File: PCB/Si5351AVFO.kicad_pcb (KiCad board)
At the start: 4 copper layers, 100 x 65 mm, 127 parts, among them J1 USB_C_Receptacle, J2 SMA CLK0, J3 SMA CLK1, J4 SMA CLK2, J5 UPDI, SW1 EC11E18244A5, SW2 BAND, SW3 STEP, SW4 MENU, U1 LP2985-3.3, U2 Si5351A-B-GT, U3 CP2102N-A02-GQFN24, U4 ATtiny3226-SU, U5 LP2985-3.3, X1 25MHz TCXO

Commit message: WIP: partial PCB review fixes (interrupted pass)
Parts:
- added C26: 100n, Capacitor_SMD:C_0402_1005Metric, F.Cu at (172.5, 131.4)
- added C27: 10u, Capacitor_SMD:C_0805_2012Metric, F.Cu at (182.3, 134.6)
- added C28: 100n, Capacitor_SMD:C_0805_2012Metric, F.Cu at (182.3, 136.6)
- added FID1: Fiducial, Fiducial:Fiducial_1mm_Mask2mm, F.Cu at (103.0, 109.0)
- added FID2: Fiducial, Fiducial:Fiducial_1mm_Mask2mm, F.Cu at (196.0, 140.0)
- added FID3: Fiducial, Fiducial:Fiducial_1mm_Mask2mm, F.Cu at (104.0, 152.0)
- R100, R120, R140: footprint Resistor_SMD:R_0805_2012Metric -> Resistor_SMD:R_0402_1005Metric
- SW2: value BAND -> SOFT1
- SW3: value STEP -> SOFT2
- SW4: value MENU -> SOFT3
- moved R100 11.0 mm to (169.0, 132.2), turned to 180 degrees
- moved R140 9.12 mm to (174.9, 131.9)
- moved C4 2.51 mm to (169.6, 136.2), turned to 90 degrees
- moved R120 2.49 mm to (171.0, 131.5)
- moved D1 1.90 mm to (116.0, 110.3)
- moved U2 1.56 mm to (172.0, 135.3), turned to 90 degrees
- turned C6 to -90 degrees
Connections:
- net /MCU and UI/BTN_BAND renamed /MCU and UI/BTN_S1
- net /MCU and UI/BTN_BAND_SW renamed /MCU and UI/BTN_S1_SW
- net /MCU and UI/BTN_MENU renamed /MCU and UI/BTN_S3
- net /MCU and UI/BTN_MENU_SW renamed /MCU and UI/BTN_S3_SW
- net /MCU and UI/BTN_STEP renamed /MCU and UI/BTN_S2
- net /MCU and UI/BTN_STEP_SW renamed /MCU and UI/BTN_S2_SW
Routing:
- net +3V3_CLK: track 55.2 -> 30.2 mm, vias 2 -> 5
- net I2C_SDA: track 55.4 -> 33.7 mm, vias 3 -> 2
- net /Synth and RF outputs/CLK0: track 22.8 -> 2.44 mm, vias 2 -> 0
- net +3V3D: track 138.3 -> 119.5 mm
- net /Synth and RF outputs/CLK2: track 15.9 -> 2.16 mm, vias 2 -> 0
- net +5V: track 79.9 -> 68.9 mm, vias 2 -> 0
- net /Power and USB/CP_RST: track 12.1 -> 1.94 mm, vias 3 -> 0
- net /Power and USB/CP_VBUS_SENSE: track 11.5 -> 1.40 mm, vias 2 -> 0
- net Net-(C100-Pad1): track 2.96 -> 12.3 mm
- net I2C_SCL: track 35.7 -> 44.8 mm
- net /Power and USB/USB_DP: track 17.6 -> 25.9 mm
- net /MCU and UI/ENC_B: track 9.59 -> 17.5 mm, vias 0 -> 2
- net Net-(C140-Pad1): track 2.96 -> 10.0 mm
- net /MCU and UI/BTN_S3_SW: track 29.5 -> 22.7 mm
- net MCU_TX: track 59.8 -> 65.9 mm
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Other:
- board text added: "Controlled impedance 50 ohm, L1/L2, 0.31/0.20 (CPWG, RF50) per JLC calculator"
- board text added: "FAB NOTES: JLC04161H-7628 4L 1.6mm, 1oz outer"
- board text added: "U3 thermal-pad vias: tented both sides + filled (epoxy)"

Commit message: PCB: C27 10u/C28 100n at FB1 output (+3V3_CLK), reroute +3V3_CLK FB1->U2 on In2/B.Cu; C26 at VDDO pin 7, C4 at VDD pin 1
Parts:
- moved C27 48.5 mm to (143.9, 104.9)
- moved C28 48.4 mm to (143.9, 107.0)
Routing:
- net +3V3_CLK: track 30.2 -> 66.0 mm
- net GND: track 65.2 -> 67.2 mm, vias 320 -> 318
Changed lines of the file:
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@@
 	(footprint "Capacitor_SMD:C_0805_2012Metric"
 		(layer "F.Cu")
-		(at 182.3 134.6)
+		(at 143.95 104.9)
 		(descr "Capacitor SMD 0805 (2012 Metric), square (rectangular) end terminal, IPC-7351 nominal, (Body size source: IPC-SM-782 page 76, https://www.pcb-3d.com/wordpress/wp-content/uploads/ipc-sm-782a_amendment_1_and_2.pdf, https://docs.google.com/spreadsheets/d/1BsfQQcO9C6DZCsRaXUlFlo91Tg2WpOkGARC1WS5S8t0/edit?usp=sharing)")
 		(tags "capacitor")
@@
 	(footprint "Capacitor_SMD:C_0805_2012Metric"
 		(layer "F.Cu")
-		(at 182.3 136.6)
+		(at 143.95 107)
 		(descr "Capacitor SMD 0805 (2012 Metric), square (rectangular) end terminal, IPC-7351 nominal, (Body size source: IPC-SM-782 page 76, https://www.pcb-3d.com/wordpress/wp-content/uploads/ipc-sm-782a_amendment_1_and_2.pdf, https://docs.google.com/spreadsheets/d/1BsfQQcO9C6DZCsRaXUlFlo91Tg2WpOkGARC1WS5S8t0/edit?usp=sharing)")
 		(tags "capacitor")
@@
 	)
 	(segment
+		(start 144.9 107)
+		(end 145.9 107)
+		(width 0.4)
+		(layer "F.Cu")
+		(net "GND")
+	)
+	(segment
 		(start 138.45 114)
 		(end 139.399999 114)
@@
 	)
 	(segment
+		(start 144.9 104.9)
+		(end 145.9 104.9)
+		(width 0.4)
+		(layer "F.Cu")
+		(net "GND")
+	)
+	(segment
 		(start 136.2 163.25)
 		(end 134.75 163.25)
@@
 	)
 	(via
-		(at 184.799999 133.8)
-		(size 0.6)
-		(drill 0.3)
-		(layers "F.Cu" "B.Cu")
-		(locked yes)
-		(net "GND")
-	)
-	(via
 		(at 176.799999 137)
 		(size 0.6)
@@
 	)
 	(via
-		(at 184.2 134.6)
-		(size 0.6)
-		(drill 0.3)
-		(layers "F.Cu" "B.Cu")
-		(locked yes)
-		(net "GND")
-	)
-	(via
 		(at 179.125 111.25)
 		(size 0.6)
@@
 	)
 	(via
+		(at 145.9 104.9)
+		(size 0.6)
+		(drill 0.3)
+		(layers "F.Cu" "B.Cu")
+		(net "GND")
+	)
+	(via
 		(at 179.999999 117.8)
 		(size 0.6)
@@
 	)
 	(via
+		(at 145.9 107)
+		(size 0.6)
+		(drill 0.3)
+		(layers "F.Cu" "B.Cu")
+		(net "GND")
+	)
+	(via
 		(at 165.6 117.8)
 		(size 0.6)
@@
 	)
 	(via
-		(at 184.799999 135.4)
-		(size 0.6)
-		(drill 0.3)
-		(layers "F.Cu" "B.Cu")
-		(locked yes)
-		(net "GND")
-	)
-	(via
 		(at 167.2 125.8)
 		(size 0.6)
@@
 	)
 	(via
-		(at 184.2 136.6)
-		(size 0.6)
-		(drill 0.3)
-		(layers "F.Cu" "B.Cu")
-		(locked yes)
-		(net "GND")
-	)
-	(via
 		(at 156 109.8)
 		(size 0.6)
@@
 	)
 	(segment
-		(start 180.1 135.6)
-		(end 181.35 135.6)
-		(width 0.4)
-		(locked yes)
-		(layer "F.Cu")
-		(net "+3V3_CLK")
-	)
-	(segment
-		(start 143 110.2125)
-		(end 143 109.325)
+		(start 143 110.21)
+		(end 143 104.9)
 		(width 0.4)
-		(locked yes)
 		(layer "F.Cu")
 		(net "+3V3_CLK")
@@
 	)
 	(segment
-		(start 181.35 134.6)
-		(end 181.35 136.6)
+		(start 143 104.9)
+		(end 143 103.6)
 		(width 0.4)
-		(locked yes)
 		(layer "F.Cu")
 		(net "+3V3_CLK")
@@
 	)
 	(via
-		(at 168.4 137.4)
+		(at 154.6 126.6)
 		(size 0.6)
 		(drill 0.3)
 		(layers "F.Cu" "B.Cu")
-		(locked yes)
 		(net "+3V3_CLK")
 	)
 	(via
-		(at 180.1 135.6)
+		(at 143 103.6)
 		(size 0.6)
 		(drill 0.3)
 		(layers "F.Cu" "B.Cu")
-		(locked yes)
 		(net "+3V3_CLK")
 	)
 	(via
-		(at 163.65 135.15)
+		(at 168.4 137.4)
 		(size 0.6)
 		(drill 0.3)
@@
 	)
 	(via
-		(at 143 109.325)
+		(at 163.65 135.15)
 		(size 0.6)
 		(drill 0.3)
@@
 	)
 	(segment
+		(start 160 132.6)
+		(end 161.2 132.6)
+		(width 0.3)
+		(layer "B.Cu")
+		(net "+3V3_CLK")
+	)
+	(segment
+		(start 159 131.4)
+		(end 159 131.6)
+		(width 0.3)
+		(layer "B.Cu")
+		(net "+3V3_CLK")
+	)
+	(segment
+		(start 154.6 126.6)
+		(end 159 131.4)
+		(width 0.3)
+		(layer "B.Cu")
+		(net "+3V3_CLK")
+	)
+	(segment
+		(start 159 131.6)
+		(end 160 132.6)
+		(width 0.3)
+		(layer "B.Cu")
+		(net "+3V3_CLK")
+	)
+	(segment
+		(start 163.4 135)
+		(end 163.6 135.2)
+		(width 0.3)
+		(layer "B.Cu")
+		(net "+3V3_CLK")
+	)
+	(segment
+		(start 161.2 132.6)
+		(end 163.4 134.8)
+		(width 0.3)
+		(layer "B.Cu")
+		(net "+3V3_CLK")
+	)
+	(segment
+		(start 163.4 134.8)
+		(end 163.4 135)
+		(width 0.3)
+		(layer "B.Cu")
+		(net "+3V3_CLK")
+	)
+	(segment
+		(start 147.2 108)
+		(end 150.8 111.6)
+		(width 0.3)
+		(layer "In2.Cu")
+		(net "+3V3_CLK")
+	)
+	(segment
+		(start 153.6 125.4)
+		(end 153.6 126.6)
+		(width 0.3)
+		(layer "In2.Cu")
+		(net "+3V3_CLK")
+	)
+	(segment
+		(start 152.4 124.2)
+		(end 153.6 125.4)
+		(width 0.3)
+		(layer "In2.Cu")
+		(net "+3V3_CLK")
+	)
+	(segment
+		(start 146 106.2)
+		(end 146.2 106.4)
+		(width 0.3)
+		(layer "In2.Cu")
+		(net "+3V3_CLK")
+	)
+	(segment
 		(start 163.65 135.15)
 		(end 166.15 135.15)
@@
 	)
 	(segment
-		(start 172.7446 134.3554)
-		(end 172.5 134.6)
+		(start 153.6 126.6)
+		(end 154.6 126.6)
 		(width 0.3)
 		(layer "In2.Cu")
@@
 	)
 	(segment
-		(start 175.7767 134.5101)
-		(end 174.4899 134.5101)
+		(start 145.6 106.2)
+		(end 146 106.2)
 		(width 0.3)
 		(layer "In2.Cu")
@@
 	)
 	(segment
-		(start 174.4899 134.5101)
-		(end 174.2177 134.2379)
+		(start 166.15 135.15)
+		(end 168.4 137.4)
 		(width 0.3)
 		(layer "In2.Cu")
@@
 	)
 	(segment
-		(start 166.15 135.15)
-		(end 168.4 137.4)
+		(start 146.2 106.4)
+		(end 146.4 106.4)
 		(width 0.3)
 		(layer "In2.Cu")
@@
 	)
 	(segment
-		(start 178.9202 134.4202)
-		(end 175.8666 134.4202)
+		(start 168.4 137.4)
+		(end 171.2 134.6)
 		(width 0.3)
 		(layer "In2.Cu")
@@
 	)
 	(segment
-		(start 174.2177 134.2379)
-		(end 173.8851 134.2379)
-		(width 0.225)
+		(start 152.4 124)
+		(end 152.4 124.2)
+		(width 0.3)
 		(layer "In2.Cu")
 		(net "+3V3_CLK")
 	)
 	(segment
-		(start 173.8851 134.2379)
-		(end 173.7676 134.3554)
-		(width 0.225)
+		(start 143 103.6)
+		(end 145.6 106.2)
+		(width 0.3)
 		(layer "In2.Cu")
 		(net "+3V3_CLK")
 	)
 	(segment
-		(start 180.1 135.6)
-		(end 178.9202 134.4202)
+		(start 147.2 107.2)
+		(end 147.2 108)
 		(width 0.3)
 		(layer "In2.Cu")
@@
 	)
 	(segment
-		(start 168.4 137.4)
-		(end 171.2 134.6)
+		(start 150.8 122.4)
+		(end 152.4 124)
 		(width 0.3)
 		(layer "In2.Cu")
@@
 	)
 	(segment
-		(start 173.7676 134.3554)
-		(end 172.7446 134.3554)
+		(start 146.4 106.4)
+		(end 147.2 107.2)
 		(width 0.3)
 		(layer "In2.Cu")
@@
 	)
 	(segment
-		(start 175.8666 134.4202)
-		(end 175.7767 134.5101)
+		(start 150.8 111.6)
+		(end 150.8 122.4)
 		(width 0.3)
 		(layer "In2.Cu")

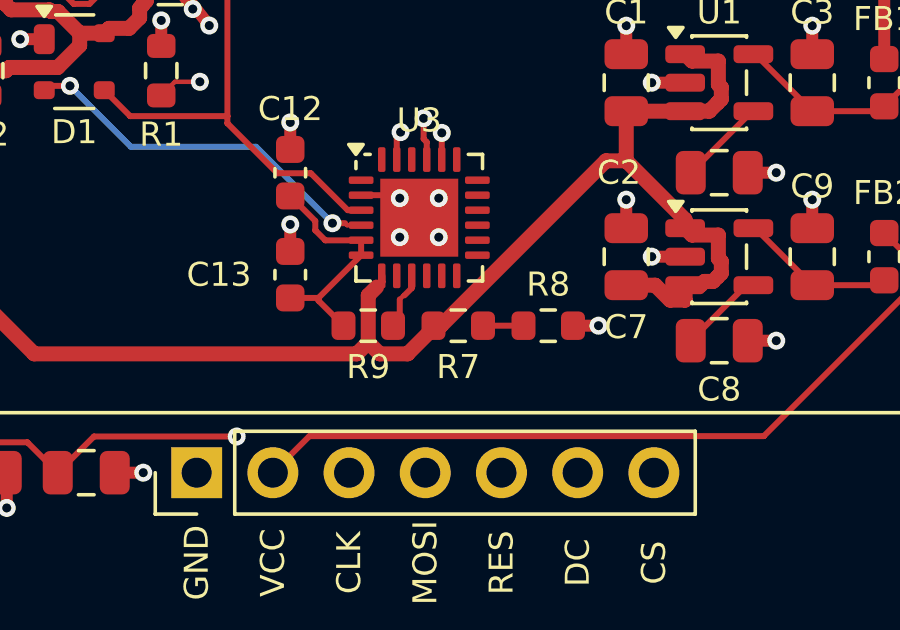
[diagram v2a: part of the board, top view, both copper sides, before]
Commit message: PCB: connect CP_VBUS_SENSE (U3.8) via B.Cu hop, tighten CP_RST escape; DRC 0 unconnected, 0 clearance
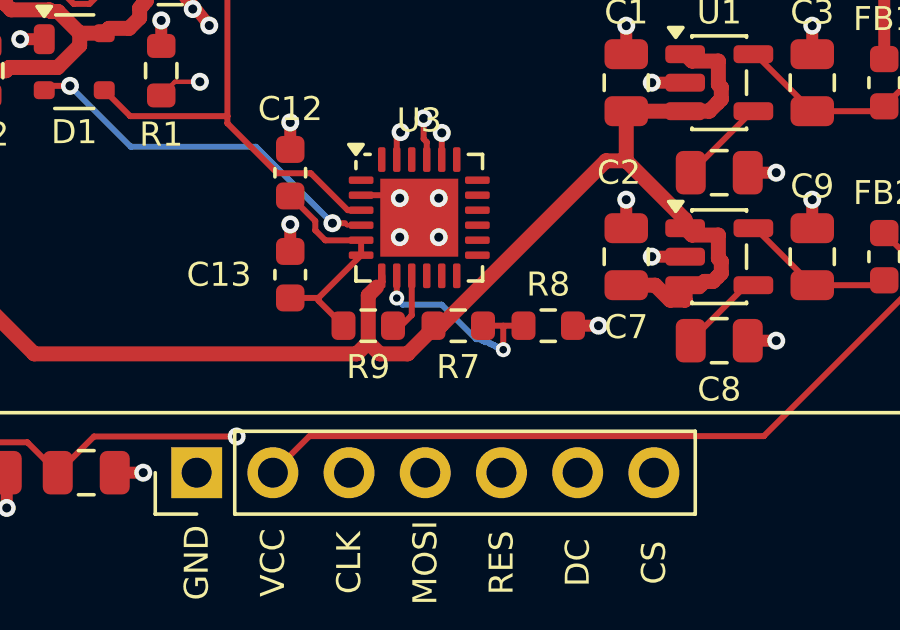
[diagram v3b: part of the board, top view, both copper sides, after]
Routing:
- net /Power and USB/CP_VBUS_SENSE: track 1.40 -> 7.23 mm, vias 0 -> 2
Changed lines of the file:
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@@
+	)
+	(segment
+		(start 126.75 117.44)
+		(end 126.75 118.18)
+		(width 0.2)
+		(layer "F.Cu")
+		(net "/Power and USB/CP_VBUS_SENSE")
 	)
 	(segment
@@
 		(width 0.2)
 		(layer "F.Cu")
+		(net "/Power and USB/CP_VBUS_SENSE")
+	)
+	(segment
+		(start 130.3 119.1)
+		(end 130.3 119.9)
+		(width 0.2)
+		(layer "F.Cu")
+		(net "/Power and USB/CP_VBUS_SENSE")
+	)
+	(via
+		(at 130.3 119.9)
+		(size 0.5)
+		(drill 0.25)
+		(layers "F.Cu" "B.Cu")
+		(net "/Power and USB/CP_VBUS_SENSE")
+	)
+	(via
+		(at 126.75 118.18)
+		(size 0.5)
+		(drill 0.25)
+		(layers "F.Cu" "B.Cu")
+		(net "/Power and USB/CP_VBUS_SENSE")
+	)
+	(segment
+		(start 130 119.75)
+		(end 130.05 119.8)
+		(width 0.2)
+		(layer "B.Cu")
+		(net "/Power and USB/CP_VBUS_SENSE")
+	)
+	(segment
+		(start 129.9 119.7)
+		(end 129.949999 119.75)
+		(width 0.2)
+		(layer "B.Cu")
+		(net "/Power and USB/CP_VBUS_SENSE")
+	)
+	(segment
+		(start 126.95 118.4)
+		(end 128.25 118.4)
+		(width 0.2)
+		(layer "B.Cu")
+		(net "/Power and USB/CP_VBUS_SENSE")
+	)
+	(segment
+		(start 126.8 118.3)
+		(end 126.85 118.3)
+		(width 0.2)
+		(layer "B.Cu")
+		(net "/Power and USB/CP_VBUS_SENSE")
+	)
+	(segment
+		(start 129.699999 119.65)
+		(end 129.8 119.65)
+		(width 0.2)
+		(layer "B.Cu")
+		(net "/Power and USB/CP_VBUS_SENSE")
+	)
+	(segment
+		(start 130.1 119.8)
+		(end 130.15 119.85)
+		(width 0.2)
+		(layer "B.Cu")
+		(net "/Power and USB/CP_VBUS_SENSE")
+	)
+	(segment
+		(start 130.25 119.85)
+		(end 130.3 119.9)
+		(width 0.2)
+		(layer "B.Cu")
+		(net "/Power and USB/CP_VBUS_SENSE")
+	)
+	(segment
+		(start 129.6 119.6)
+		(end 129.65 119.6)
+		(width 0.2)
+		(layer "B.Cu")
+		(net "/Power and USB/CP_VBUS_SENSE")
+	)
+	(segment
+		(start 130.15 119.85)
+		(end 130.25 119.85)
+		(width 0.2)
+		(layer "B.Cu")
+		(net "/Power and USB/CP_VBUS_SENSE")
+	)
+	(segment
+		(start 126.85 118.3)
+		(end 126.95 118.4)
+		(width 0.2)
+		(layer "B.Cu")
+		(net "/Power and USB/CP_VBUS_SENSE")
+	)
+	(segment
+		(start 128.25 118.4)
+		(end 129.4 119.55)
+		(width 0.2)
+		(layer "B.Cu")
+		(net "/Power and USB/CP_VBUS_SENSE")
+	)
+	(segment
+		(start 126.75 118.18)
+		(end 126.8 118.3)
+		(width 0.2)
+		(layer "B.Cu")
+		(net "/Power and USB/CP_VBUS_SENSE")
+	)
+	(segment
+		(start 129.55 119.55)
+		(end 129.6 119.6)
+		(width 0.2)
+		(layer "B.Cu")
+		(net "/Power and USB/CP_VBUS_SENSE")
+	)
+	(segment
+		(start 129.8 119.65)
+		(end 129.85 119.7)
+		(width 0.2)
+		(layer "B.Cu")
+		(net "/Power and USB/CP_VBUS_SENSE")
+	)
+	(segment
+		(start 129.85 119.7)
+		(end 129.9 119.7)
+		(width 0.2)
+		(layer "B.Cu")
+		(net "/Power and USB/CP_VBUS_SENSE")
+	)
+	(segment
+		(start 129.65 119.6)
+		(end 129.699999 119.65)
+		(width 0.2)
+		(layer "B.Cu")
+		(net "/Power and USB/CP_VBUS_SENSE")
+	)
+	(segment
+		(start 129.949999 119.75)
+		(end 130 119.75)
+		(width 0.2)
+		(layer "B.Cu")
+		(net "/Power and USB/CP_VBUS_SENSE")
+	)
+	(segment
+		(start 130.05 119.8)
+		(end 130.1 119.8)
+		(width 0.2)
+		(layer "B.Cu")
+		(net "/Power and USB/CP_VBUS_SENSE")
+	)
+	(segment
+		(start 129.4 119.55)
+		(end 129.55 119.55)
+		(width 0.2)
+		(layer "B.Cu")
 		(net "/Power and USB/CP_VBUS_SENSE")
 	)
@@
 	)
 	(segment
-		(start 126.625 119.1)
-		(end 126.8496 118.8754)
+		(start 127.25 117.44)
+		(end 127.25 118.75)
 		(width 0.2)
 		(layer "F.Cu")
@@
 	)
 	(segment
-		(start 126.9804 118.0905)
-		(end 127.0056 118.0905)
-		(width 0.15)
+		(start 127.25 118.75)
+		(end 126.9 119.1)
+		(width 0.2)
 		(layer "F.Cu")
 		(net "/Power and USB/CP_RST")
 	)
 	(segment
-		(start 126.8496 118.2213)
-		(end 126.9804 118.0905)
-		(width 0.15)
-		(layer "F.Cu")
-		(net "/Power and USB/CP_RST")
-	)
-	(segment
-		(start 127.0056 118.0905)
-		(end 127.25 117.8461)
-		(width 0.2)
-		(layer "F.Cu")
-		(net "/Power and USB/CP_RST")
-	)
-	(segment
-		(start 127.25 117.8461)
-		(end 127.25 117.4375)
-		(width 0.2)
-		(layer "F.Cu")
-		(net "/Power and USB/CP_RST")
-	)
-	(segment
-		(start 126.8496 118.8754)
-		(end 126.8496 118.2213)
-		(width 0.2)
-		(layer "F.Cu")
+		(start 126.9 119.1)
+		(end 126.625 119.1)
+		(width 0.2)
+		(layer "F.Cu")

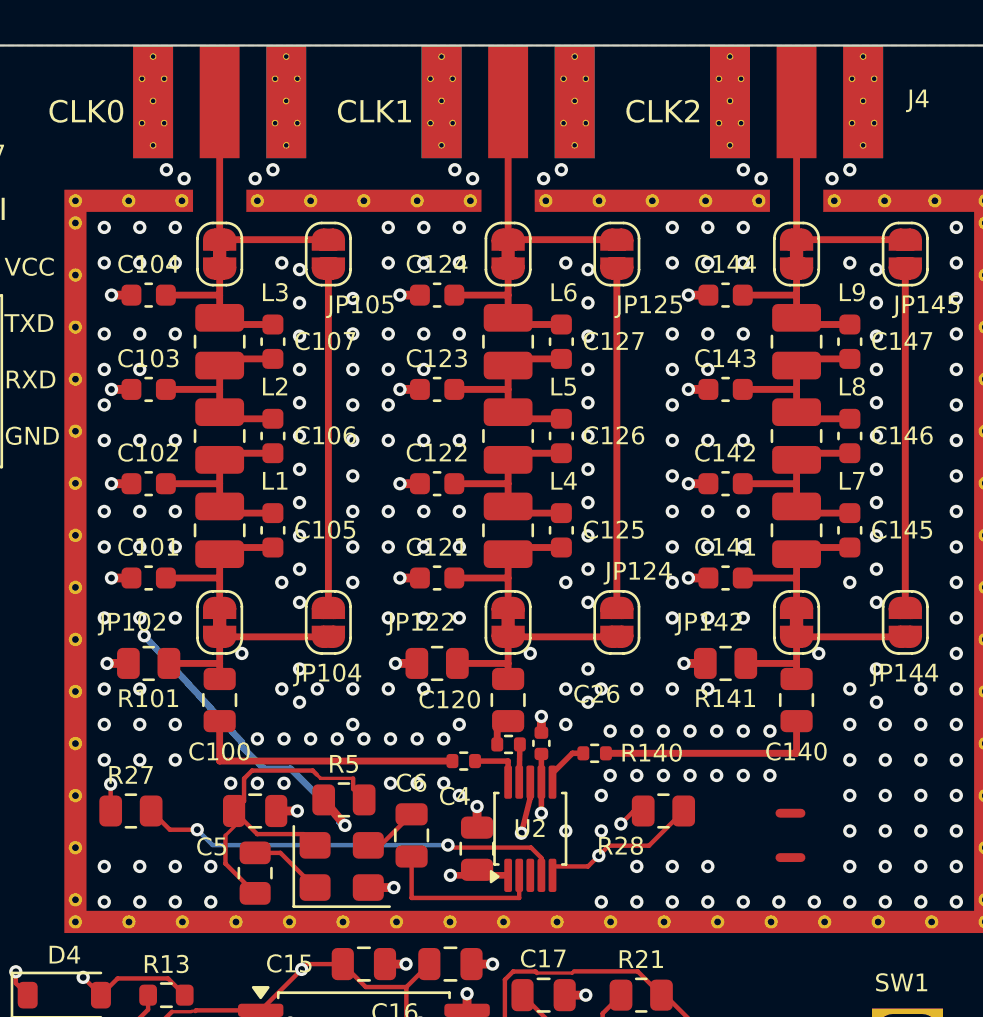
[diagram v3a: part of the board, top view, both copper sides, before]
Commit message: PCB: GND stitching - 18 vias (0.5/0.25) flanking each SMA launch cutout, 20 vias closing >2.2 mm gaps on filter fence lines
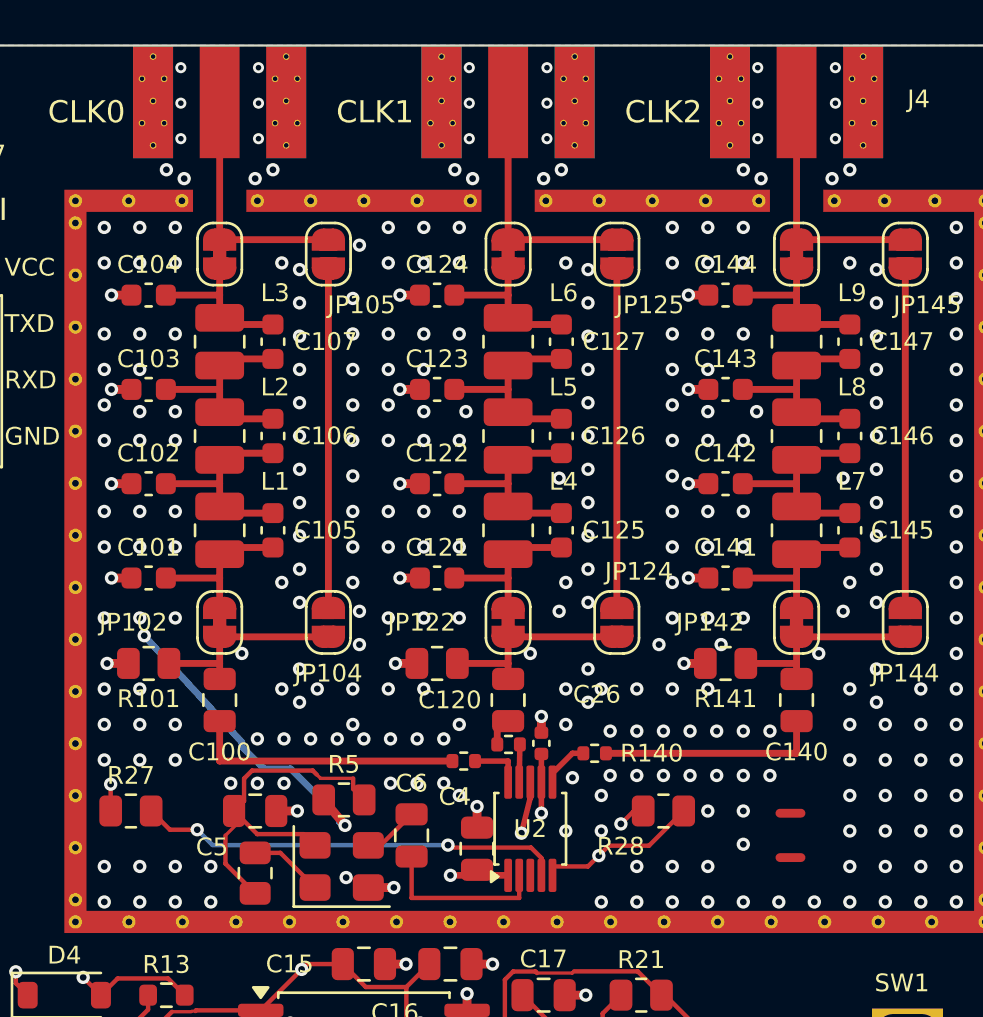
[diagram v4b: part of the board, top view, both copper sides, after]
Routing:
- net GND: vias 318 -> 356
